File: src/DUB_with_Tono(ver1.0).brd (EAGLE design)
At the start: 66 x 21.6 mm, 3 parts

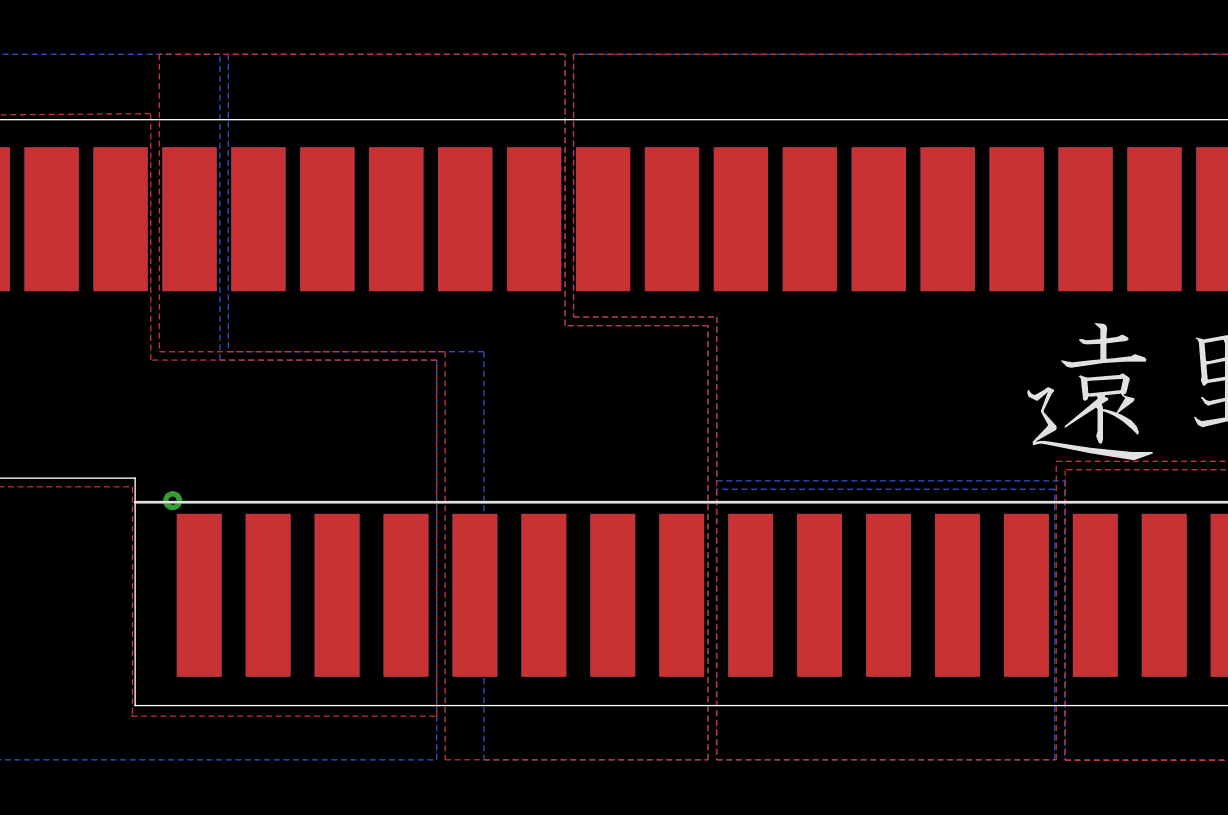
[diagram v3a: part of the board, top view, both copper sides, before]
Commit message: ビアの追加
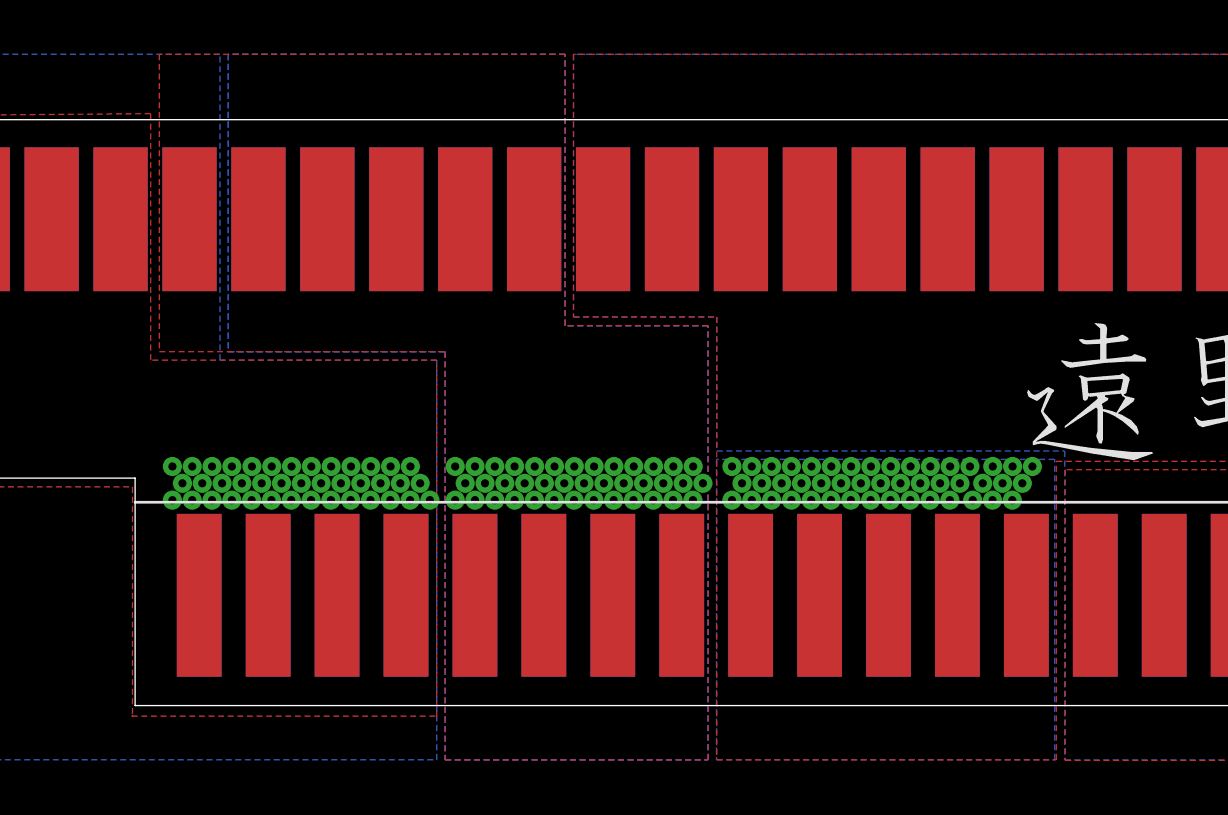
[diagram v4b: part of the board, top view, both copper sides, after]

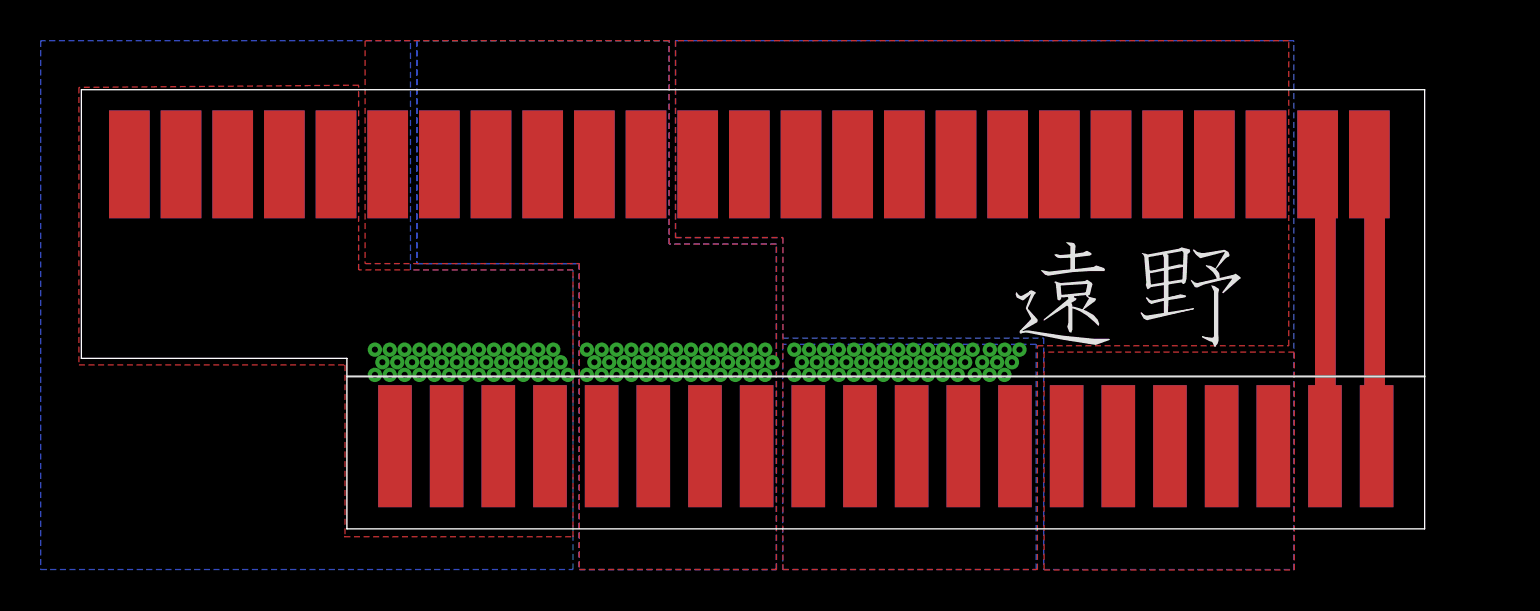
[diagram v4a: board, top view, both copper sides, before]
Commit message: Eagle移行前_基板配線完成
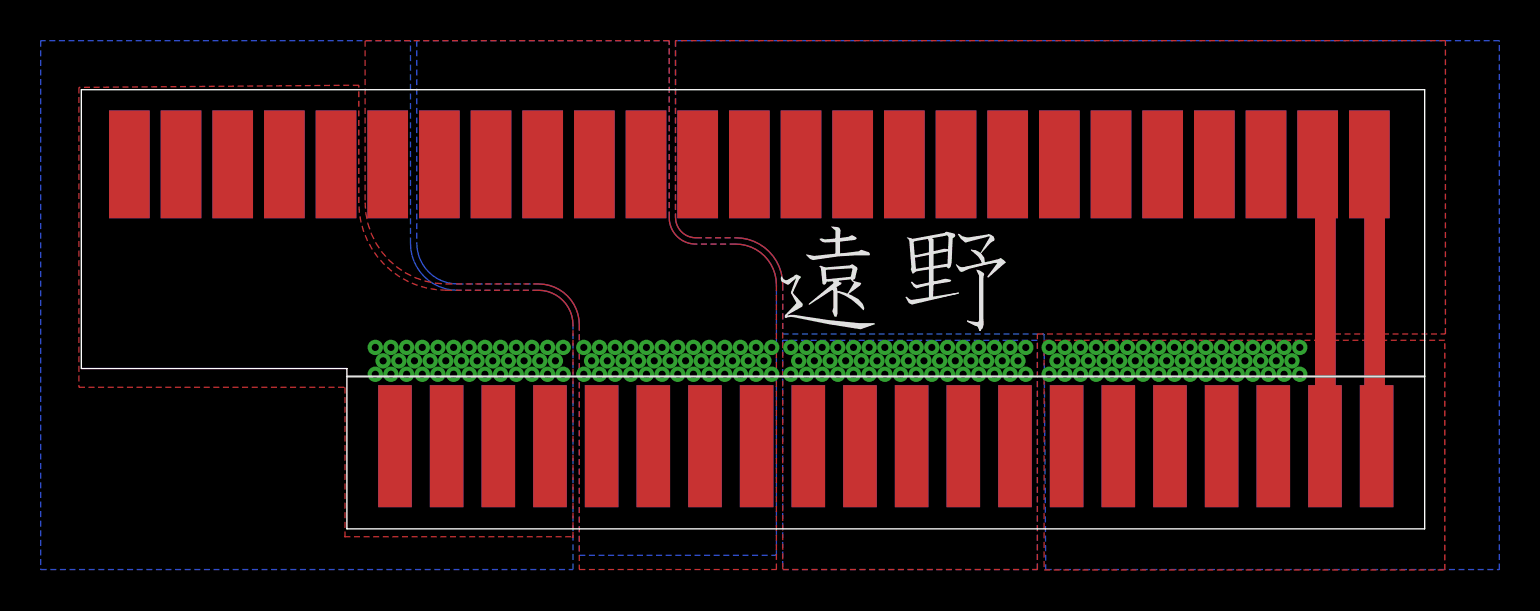
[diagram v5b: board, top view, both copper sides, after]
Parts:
- moved U$1 11.6 mm to (33.5, 9.10)
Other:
- outline, holes or cut-outs redrawn

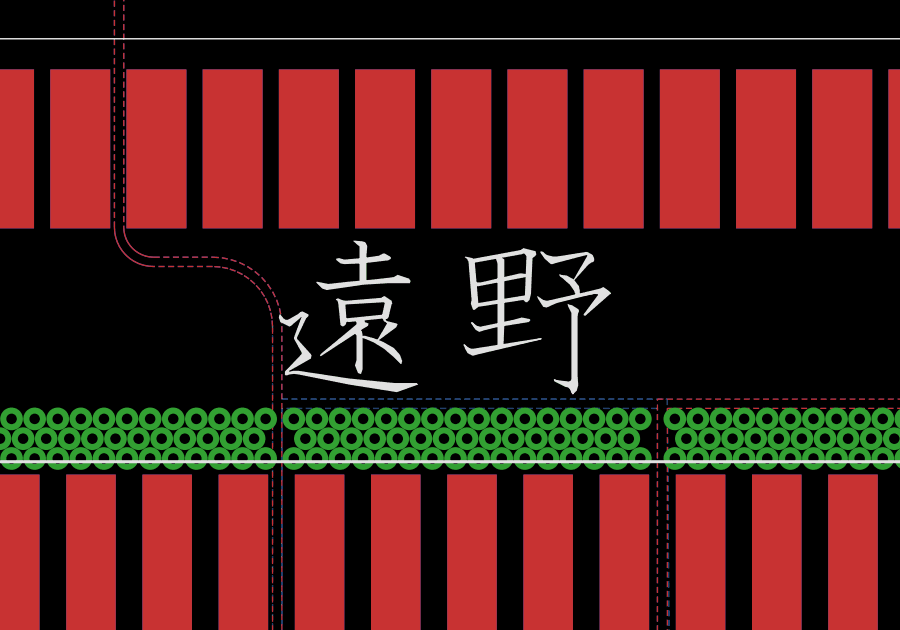
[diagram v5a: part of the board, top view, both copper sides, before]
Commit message: Eagle移行前_遠野ライブラリの修正
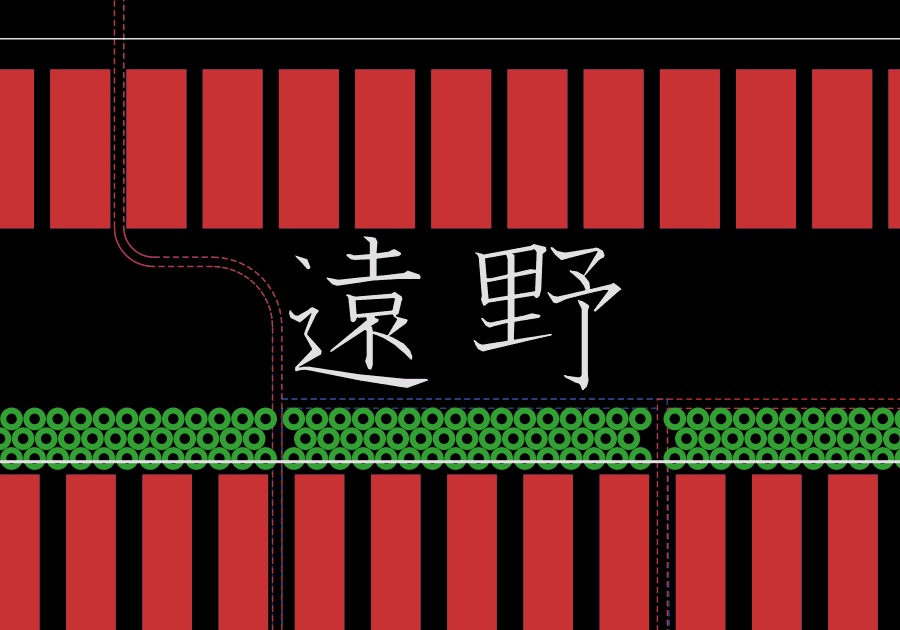
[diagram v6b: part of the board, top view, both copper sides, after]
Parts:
- moved U$1 0.37 mm to (33.9, 9.24)
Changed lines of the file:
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@@
 <element name="DUB" library="10046971-019LF" package="10046971-019LF" value="10046971-019LF" x="32.84" y="17.92" smashed="yes"/>
 <element name="遠野" library="5-5530843-4" package="5-5530843-4" value="5-5530843-4" x="40.8178" y="4.064" smashed="yes"/>
-<element name="U$1" library="OKUDA_libraries" package="TOONO" value="YAJU" x="33.54" y="9.1" smashed="yes"/>
+<element name="U$1" library="OKUDA_libraries" package="TOONO" value="YAJU" x="33.88" y="9.24" smashed="yes"/>
 </elements>
 <signals>
